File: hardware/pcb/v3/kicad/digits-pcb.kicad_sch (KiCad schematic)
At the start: 44 parts, among them J8 Conn_01x04, SW1 Hook_DPDT, SW2 SW_Push, U3 RP2040, U4 W25Q16JVSSIQ, U5 AMS1117-3.3, Y1 ABM8-272-T3

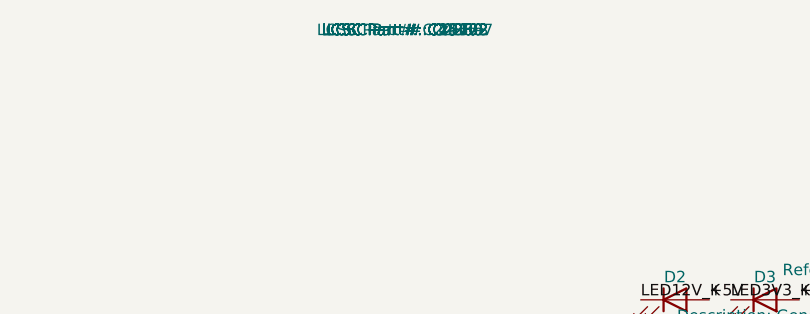
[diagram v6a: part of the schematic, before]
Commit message: fix(hardware): correct R13 to a real 120R part (C25079, was 12k C25752)
R13's LCSC field pointed at C25752, which is a 12kohm resistor, not the
120ohm the schematic value calls for. R13 sets the D3 green-LED current;
12k starves it to ~0.1mA so the indicator stays dark. Swapped to C25079
(UNI-ROYAL 0402WGF1200TCE, 120ohm) in the schematic, board, and BOM. The
in-production batch keeps the wrong part (dark D3, accepted); this fixes
the source for future runs.
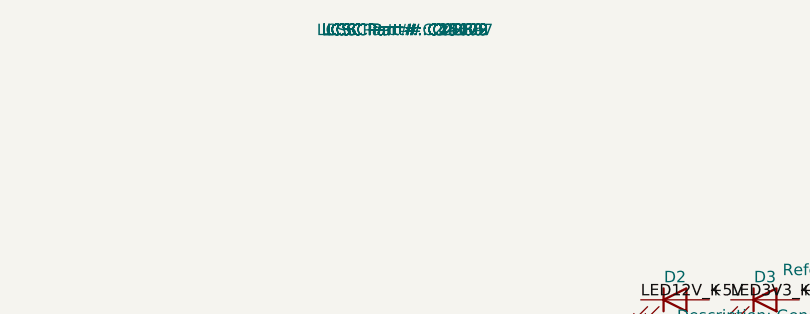
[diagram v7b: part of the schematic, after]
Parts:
- R13: LCSC Part # C25752 -> C25079
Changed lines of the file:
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@@
 			)
 		)
-		(property "LCSC Part #" "C25752"
+		(property "LCSC Part #" "C25079"
 			(at 0 0 0)
 			(show_name yes)

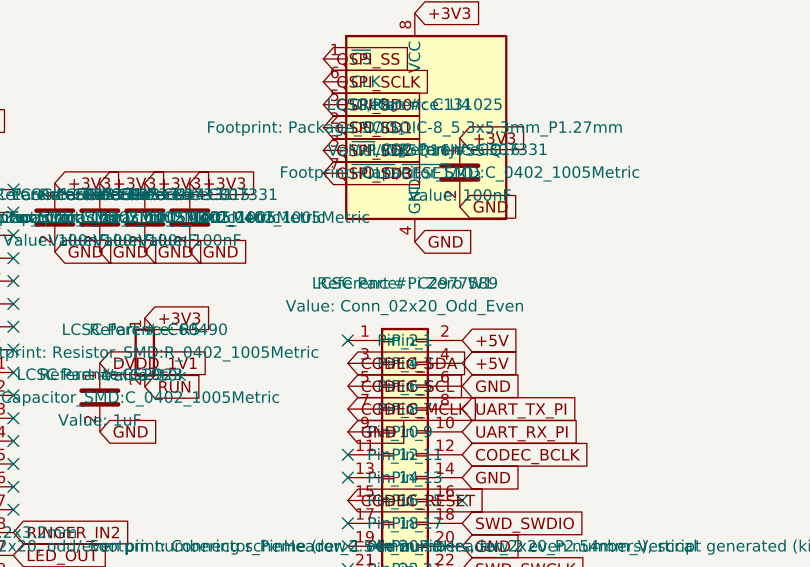
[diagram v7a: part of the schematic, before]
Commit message: fix(hardware): finalize V3 PCB for first fab (#632)
Rename the Pi header reference to PI_ZERO_W1 (the old "Pi Zero W1" had
spaces, which JLCPCB splits, breaking BOM/CPL designator matching so the
header silently dropped from assembly), correct R13 to the real 120R
part C25079, and bring the boost SW_NODE width and min-width rule, EP
ground vias, Pi-header mating mirror, and SW1 DPDT pin map into main.
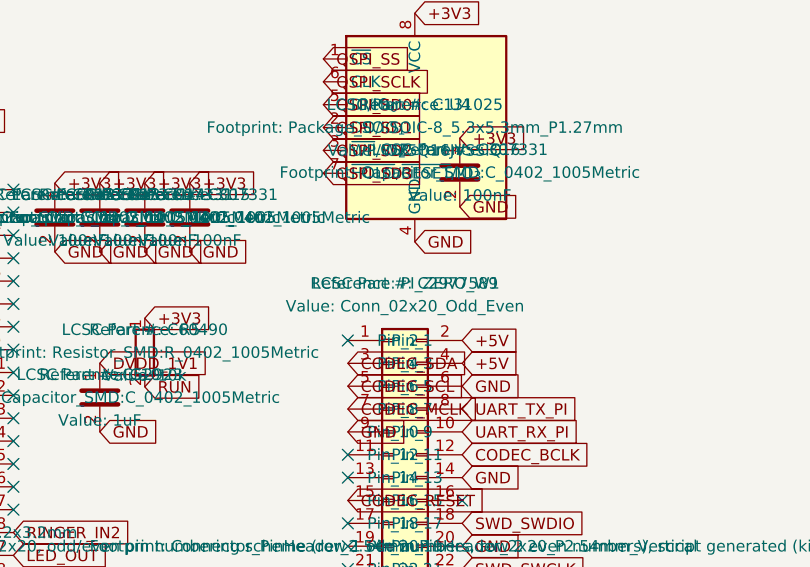
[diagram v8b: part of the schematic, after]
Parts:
- PI_ZERO_W1: renamed from Pi Zero W1
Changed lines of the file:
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@@
 		(dnp no)
 		(fields_autoplaced yes)
-		(property "Reference" "Pi Zero W1"
+		(property "Reference" "PI_ZERO_W1"
 			(at 168.91 67.31 0)
 			(show_name yes)
@@
 			(project "digits-pcb"
 				(path "/74ec24e7-a8af-4132-928f-b03228b07139"
-					(reference "Pi Zero W1")
+					(reference "PI_ZERO_W1")
 					(unit 1)
 				)
